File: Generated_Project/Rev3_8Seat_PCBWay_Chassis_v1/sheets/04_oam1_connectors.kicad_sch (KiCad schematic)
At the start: 0 parts

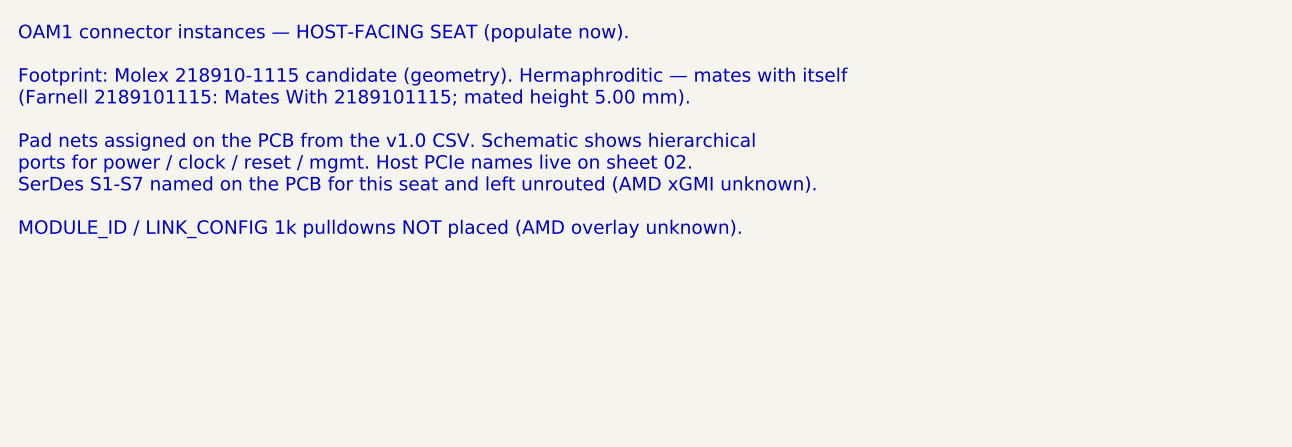
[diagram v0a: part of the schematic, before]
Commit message: Raise Rev3 chassis to 8 electrically designed seats.
Name v1.0 power/PE/clock nets on all eight OAM seats toward two DNP
PM8536B-FEI (x8 per GCD), keep SB175 star + local P48V pours, and generate
the 12-layer 2.0 mm stuffed-switch target. First stuffing may still populate
two modules; the PCB does not need a respin for the other six.

Do not fabricate. Do not energize P48V.

Co-authored-by: zivzancoeli-commits <zivzancoeli-commits@users.noreply.github.com>
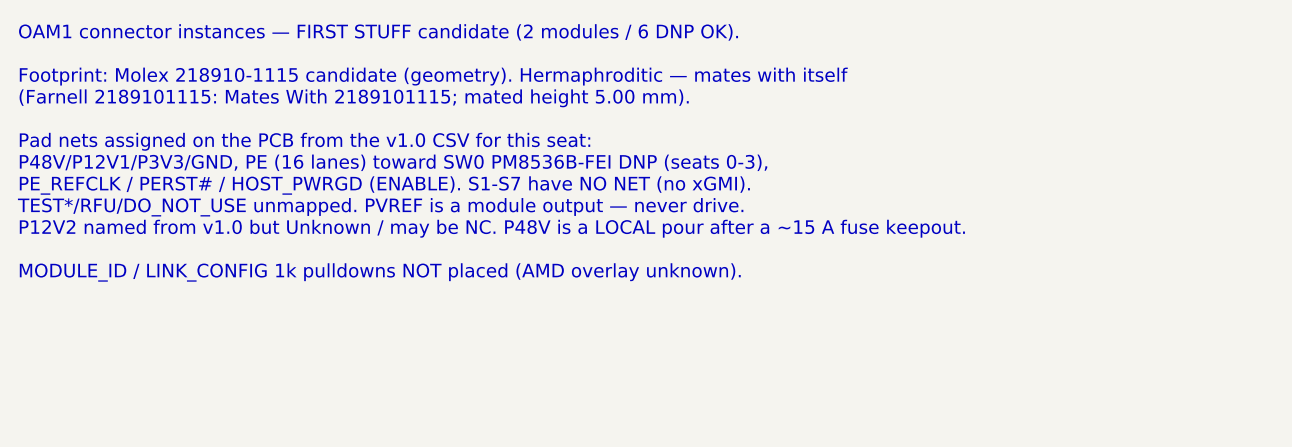
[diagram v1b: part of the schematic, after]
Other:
- note added: "OAM1 connector instances — FIRST STUFF candidate (2 modules / 6 DNP OK). Footprint: Molex 218910-1115 candidate (geometry). Hermaphroditic — mates with itself (Farnell 2189101115: Mates With 2189101115; mated height 5.00 mm). Pad nets assigned on the PCB from the v1.0 CSV for this seat: P48V/P12V1/P3V3/GND, PE (16 lanes) toward SW0 PM8536B-FEI DNP (seats 0-3), PE_REFCLK / PERST# / HOST_PWRGD (ENA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"
- note removed: "OAM1 connector instances — HOST-FACING SEAT (populate now). Footprint: Molex 218910-1115 candidate (geometry). Hermaphroditic — mates with itself (Farnell 2189101115: Mates With 2189101115; mated height 5.00 mm). Pad nets assigned on the PCB from the v1.0 CSV. Schematic shows hierarchical ports for power / clock / reset / mgmt. Host PCIe names live on sheet 02. SerDes S1-S7 named on the PCB for t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"
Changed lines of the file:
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@@
 		(date "2026-08-21")
 		(rev "Rev3_8Seat_PCBWay_v1")
-		(comment 1 "DO NOT FABRICATE. DO NOT ENERGIZE P48V. Ticket 167157 open.")
-		(comment 2 "Documentation sheet — no invented nets")
-		(comment 3 "Pin names: OAM Pin map rev 1.0.xlsx — OCP generic, NOT AMD overlay")
-		(comment 4 "r2.0 maps UNUSABLE. P3V3=2 Conn0 C1/C2. 8-seat PCBWay chassis stub.")
+        (comment 1 "DO NOT FABRICATE. DO NOT ENERGIZE P48V. Molex 60V written 2026-08-18; 1.2A/contact OPEN.")
+        (comment 2 "Documentation sheet — no invented nets")
+        (comment 3 "Pin names: OAM Pin map rev 1.0.xlsx — OCP generic, NOT AMD overlay")
+        (comment 4 "r2.0 UNUSABLE. P3V3=Conn0 C1/C2. 12L 2.0mm stuffed-switch TARGET. Star-fed P48V.")
 	)
-	(text "OAM1 connector instances — HOST-FACING SEAT (populate now).\n\nFootprint: Molex 218910-1115 candidate (geometry). Hermaphroditic — mates with itself\n(Farnell 2189101115: Mates With 2189101115; mated height 5.00 mm).\n\nPad nets assigned on the PCB from the v1.0 CSV. Schematic shows hierarchical\nports for power / clock / reset / mgmt. Host PCIe names live on sheet 02.\nSerDes S1-S7 named on the PCB for this seat and left unrouted (AMD xGMI unknown).\n\nMODULE_ID / LINK_CONFIG 1k pulldowns NOT placed (AMD overlay unknown).\n"
+	(text "OAM1 connector instances — FIRST STUFF candidate (2 modules / 6 DNP OK).\n\nFootprint: Molex 218910-1115 candidate (geometry). Hermaphroditic — mates with itself\n(Farnell 2189101115: Mates With 2189101115; mated height 5.00 mm).\n\nPad nets assigned on the PCB from the v1.0 CSV for this seat:\nP48V/P12V1/P3V3/GND, PE (16 lanes) toward SW0 PM8536B-FEI DNP (seats 0-3),\nPE_REFCLK / PERST# / HOST_PWRGD (ENABLE). S1-S7 have NO NET (no xGMI).\nTEST*/RFU/DO_NOT_USE unmapped. PVREF is a module output — never drive.\nP12V2 named from v1.0 but Unknown / may be NC. P48V is a LOCAL pour after a ~15 A fuse keepout.\n\nMODULE_ID / LINK_CONFIG 1k pulldowns NOT placed (AMD overlay unknown).\n"
 		(exclude_from_sim no)
 		(at 20.32 20.32 0)

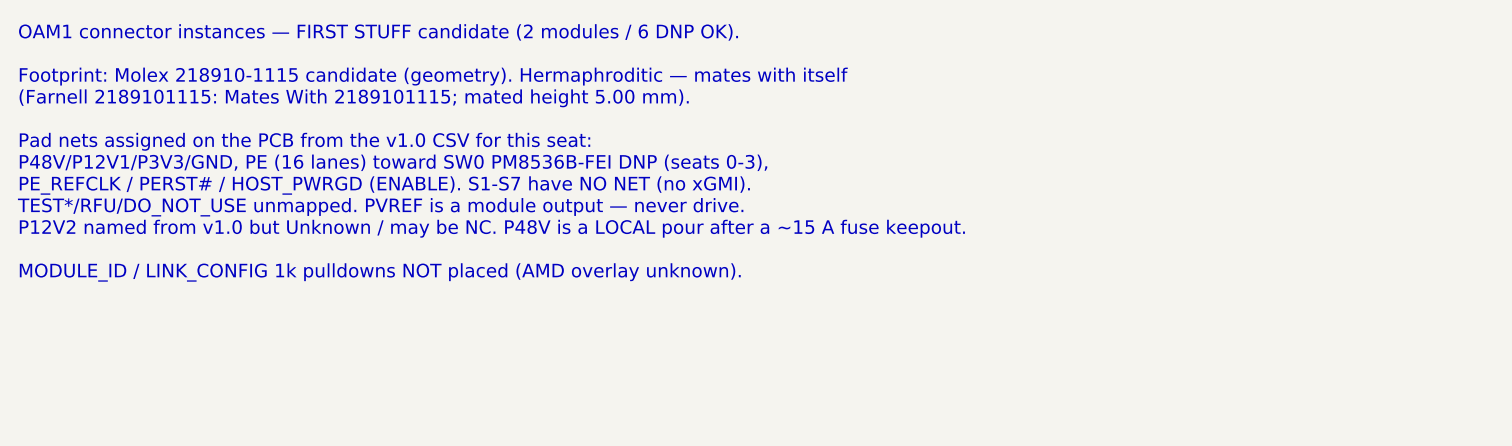
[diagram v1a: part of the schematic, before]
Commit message: Label PEX8780-AB80BI G as the only switch CANDIDATE (DNP).
Keepout is one 35 mm 1156-FCBGA for 8x x8 Gen3 plus one x16 host uplink.
Do not invent a second MPN. Do not stuff. 8-layer is likely if this BGA
is ever assembled; PCBWay 1156-FCBGA attach remains Unknown.

Still do not fabricate or energize P48V. No xGMI, no CEM.

Co-authored-by: zivzancoeli-commits <zivzancoeli-commits@users.noreply.github.com>
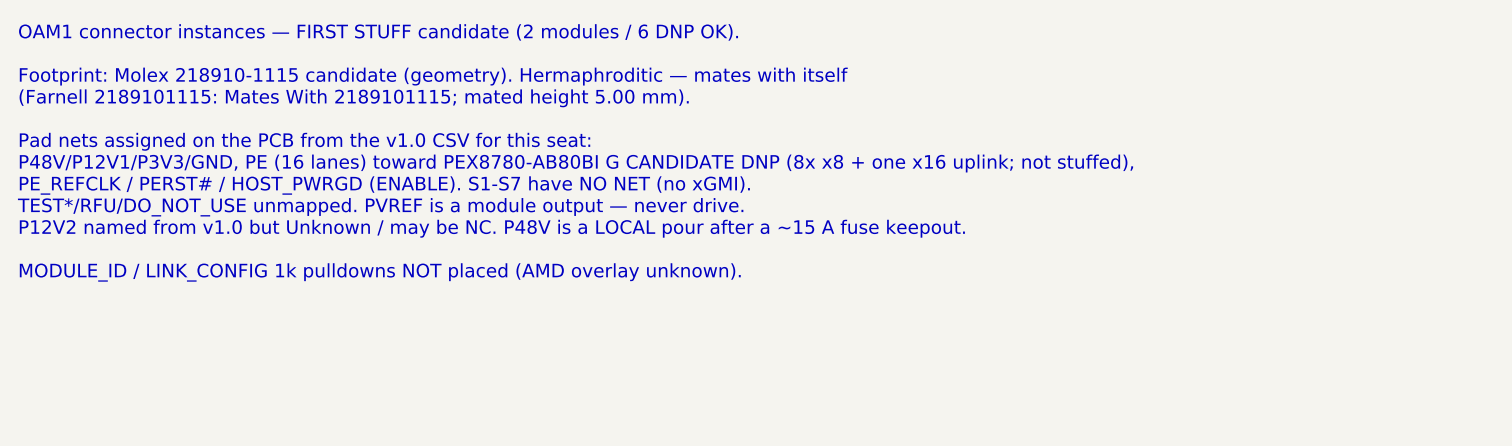
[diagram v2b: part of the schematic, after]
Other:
- note added: "OAM1 connector instances — FIRST STUFF candidate (2 modules / 6 DNP OK). Footprint: Molex 218910-1115 candidate (geometry). Hermaphroditic — mates with itself (Farnell 2189101115: Mates With 2189101115; mated height 5.00 mm). Pad nets assigned on the PCB from the v1.0 CSV for this seat: P48V/P12V1/P3V3/GND, PE (16 lanes) toward PEX8780-AB80BI G CANDIDATE DNP (8x x8 + one x16 uplink; not stuffed),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"
- note removed: "OAM1 connector instances — FIRST STUFF candidate (2 modules / 6 DNP OK). Footprint: Molex 218910-1115 candidate (geometry). Hermaphroditic — mates with itself (Farnell 2189101115: Mates With 2189101115; mated height 5.00 mm). Pad nets assigned on the PCB from the v1.0 CSV for this seat: P48V/P12V1/P3V3/GND, PE (16 lanes) toward SW0 PM8536B-FEI DNP (seats 0-3), PE_REFCLK / PERST# / HOST_PWRGD (ENA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"
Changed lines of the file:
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@@
         (comment 4 "r2.0 UNUSABLE. P3V3=Conn0 C1/C2. 12L 2.0mm stuffed-switch TARGET. Star-fed P48V.")
 	)
-	(text "OAM1 connector instances — FIRST STUFF candidate (2 modules / 6 DNP OK).\n\nFootprint: Molex 218910-1115 candidate (geometry). Hermaphroditic — mates with itself\n(Farnell 2189101115: Mates With 2189101115; mated height 5.00 mm).\n\nPad nets assigned on the PCB from the v1.0 CSV for this seat:\nP48V/P12V1/P3V3/GND, PE (16 lanes) toward SW0 PM8536B-FEI DNP (seats 0-3),\nPE_REFCLK / PERST# / HOST_PWRGD (ENABLE). S1-S7 have NO NET (no xGMI).\nTEST*/RFU/DO_NOT_USE unmapped. PVREF is a module output — never drive.\nP12V2 named from v1.0 but Unknown / may be NC. P48V is a LOCAL pour after a ~15 A fuse keepout.\n\nMODULE_ID / LINK_CONFIG 1k pulldowns NOT placed (AMD overlay unknown).\n"
+	(text "OAM1 connector instances — FIRST STUFF candidate (2 modules / 6 DNP OK).\n\nFootprint: Molex 218910-1115 candidate (geometry). Hermaphroditic — mates with itself\n(Farnell 2189101115: Mates With 2189101115; mated height 5.00 mm).\n\nPad nets assigned on the PCB from the v1.0 CSV for this seat:\nP48V/P12V1/P3V3/GND, PE (16 lanes) toward PEX8780-AB80BI G CANDIDATE DNP (8x x8 + one x16 uplink; not stuffed),\nPE_REFCLK / PERST# / HOST_PWRGD (ENABLE). S1-S7 have NO NET (no xGMI).\nTEST*/RFU/DO_NOT_USE unmapped. PVREF is a module output — never drive.\nP12V2 named from v1.0 but Unknown / may be NC. P48V is a LOCAL pour after a ~15 A fuse keepout.\n\nMODULE_ID / LINK_CONFIG 1k pulldowns NOT placed (AMD overlay unknown).\n"
 		(exclude_from_sim no)
 		(at 20.32 20.32 0)

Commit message: Make PM8536B-FEI the PRIMARY switch keepout (DNP x2).
Two 37.5 mm 1311-FCBGA courtyards, x8 per GCD (SW0 seats 0-3, SW1 4-7),
two CPU x16 uplinks. PEX8780 stays a cheaper 80-lane alt in docs only.
GCD1 = SERDES_7 remains Inferred. No CEM, no xGMI, do not fabricate.

Co-authored-by: zivzancoeli-commits <zivzancoeli-commits@users.noreply.github.com>
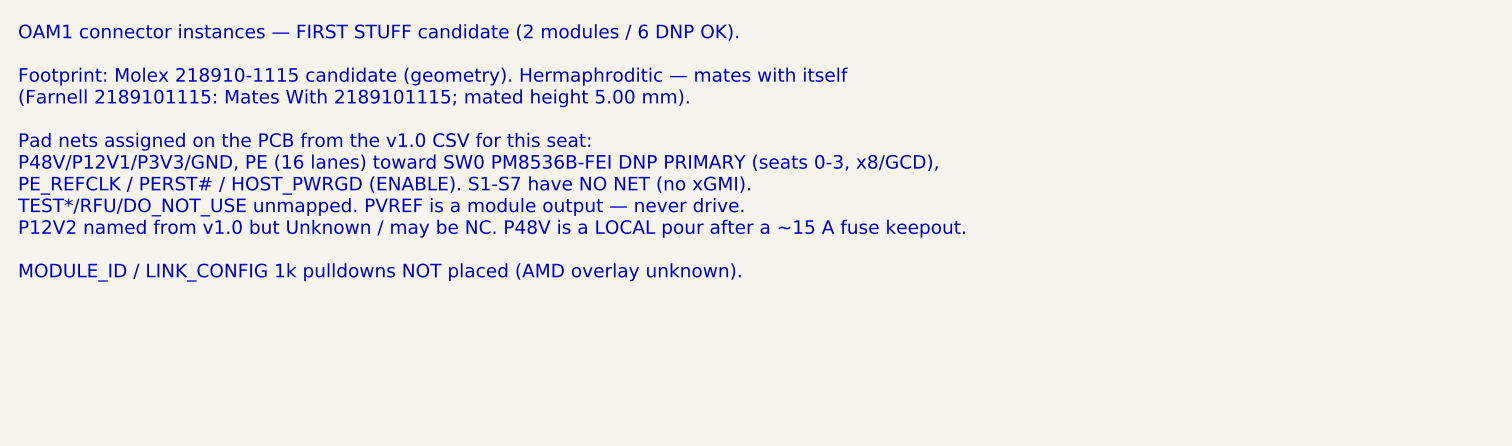
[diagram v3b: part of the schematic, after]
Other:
- note added: "OAM1 connector instances — FIRST STUFF candidate (2 modules / 6 DNP OK). Footprint: Molex 218910-1115 candidate (geometry). Hermaphroditic — mates with itself (Farnell 2189101115: Mates With 2189101115; mated height 5.00 mm). Pad nets assigned on the PCB from the v1.0 CSV for this seat: P48V/P12V1/P3V3/GND, PE (16 lanes) toward SW0 PM8536B-FEI DNP PRIMARY (seats 0-3, x8/GCD), PE_REFCLK / PERST# /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"
- note removed: "OAM1 connector instances — FIRST STUFF candidate (2 modules / 6 DNP OK). Footprint: Molex 218910-1115 candidate (geometry). Hermaphroditic — mates with itself (Farnell 2189101115: Mates With 2189101115; mated height 5.00 mm). Pad nets assigned on the PCB from the v1.0 CSV for this seat: P48V/P12V1/P3V3/GND, PE (16 lanes) toward PEX8780-AB80BI G CANDIDATE DNP (8x x8 + one x16 uplink; not stuffed),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"
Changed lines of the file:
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@@
         (comment 2 "Documentation sheet — no invented nets")
         (comment 3 "Pin names: OAM Pin map rev 1.0.xlsx — OCP generic, NOT AMD overlay")
-        (comment 4 "r2.0 UNUSABLE. P3V3=Conn0 C1/C2. 12L 2.0mm stuffed-switch TARGET. Star-fed P48V.")
+        (comment 4 "r2.0 UNUSABLE. P3V3=Conn0 C1/C2. 12L 2.0mm stuffed-switch TARGET. 2x PM8536 DNP. Star-fed P48V.")
 	)
-	(text "OAM1 connector instances — FIRST STUFF candidate (2 modules / 6 DNP OK).\n\nFootprint: Molex 218910-1115 candidate (geometry). Hermaphroditic — mates with itself\n(Farnell 2189101115: Mates With 2189101115; mated height 5.00 mm).\n\nPad nets assigned on the PCB from the v1.0 CSV for this seat:\nP48V/P12V1/P3V3/GND, PE (16 lanes) toward PEX8780-AB80BI G CANDIDATE DNP (8x x8 + one x16 uplink; not stuffed),\nPE_REFCLK / PERST# / HOST_PWRGD (ENABLE). S1-S7 have NO NET (no xGMI).\nTEST*/RFU/DO_NOT_USE unmapped. PVREF is a module output — never drive.\nP12V2 named from v1.0 but Unknown / may be NC. P48V is a LOCAL pour after a ~15 A fuse keepout.\n\nMODULE_ID / LINK_CONFIG 1k pulldowns NOT placed (AMD overlay unknown).\n"
+	(text "OAM1 connector instances — FIRST STUFF candidate (2 modules / 6 DNP OK).\n\nFootprint: Molex 218910-1115 candidate (geometry). Hermaphroditic — mates with itself\n(Farnell 2189101115: Mates With 2189101115; mated height 5.00 mm).\n\nPad nets assigned on the PCB from the v1.0 CSV for this seat:\nP48V/P12V1/P3V3/GND, PE (16 lanes) toward SW0 PM8536B-FEI DNP PRIMARY (seats 0-3, x8/GCD),\nPE_REFCLK / PERST# / HOST_PWRGD (ENABLE). S1-S7 have NO NET (no xGMI).\nTEST*/RFU/DO_NOT_USE unmapped. PVREF is a module output — never drive.\nP12V2 named from v1.0 but Unknown / may be NC. P48V is a LOCAL pour after a ~15 A fuse keepout.\n\nMODULE_ID / LINK_CONFIG 1k pulldowns NOT placed (AMD overlay unknown).\n"
 		(exclude_from_sim no)
 		(at 20.32 20.32 0)

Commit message: Make the Rev3 8-seat chassis full-width capable with four PM8536 DNP courtyards.
Same 492x372 POWER+MECH PCB; architecture is now 16 named x16 PE buses
(PE_Sn_GCD0_x16 + PE_Sn_GCD1_x16) and SW0-SW3 keepouts. Two 96-lane
switches are enough for 8x x8/GCD, not 8x x16/GCD. Host stays X11DPH-T
(~80 lanes) and cannot light 256 downstream. Do not energize P48V.

Co-authored-by: zivzancoeli-commits <zivzancoeli-commits@users.noreply.github.com>
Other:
- note added: "OAM1 connector instances — FIRST STUFF (populate path 2: seats 0-1; stuff SW0 later). Footprint: Molex 218910-1115 candidate (geometry). Hermaphroditic — mates with itself (Farnell 2189101115: Mates With 2189101115; mated height 5.00 mm). Pad nets assigned on the PCB from the v1.0 CSV for this seat: P48V/P12V1/P3V3/GND, Conn0 PE 16 lanes (PE_S1_GCD0_x16) toward SW0 PM8536B-FEI DNP (seats 0,1, 16 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"
- note removed: "OAM1 connector instances — FIRST STUFF candidate (2 modules / 6 DNP OK). Footprint: Molex 218910-1115 candidate (geometry). Hermaphroditic — mates with itself (Farnell 2189101115: Mates With 2189101115; mated height 5.00 mm). Pad nets assigned on the PCB from the v1.0 CSV for this seat: P48V/P12V1/P3V3/GND, PE (16 lanes) toward SW0 PM8536B-FEI DNP PRIMARY (seats 0-3, x8/GCD), PE_REFCLK / PERST# /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"
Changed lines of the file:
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@@
         (comment 2 "Documentation sheet — no invented nets")
         (comment 3 "Pin names: OAM Pin map rev 1.0.xlsx — OCP generic, NOT AMD overlay")
-        (comment 4 "r2.0 UNUSABLE. P3V3=Conn0 C1/C2. 12L 2.0mm stuffed-switch TARGET. 2x PM8536 DNP. Star-fed P48V.")
+        (comment 4 "r2.0 UNUSABLE. P3V3=Conn0 C1/C2. 12L 2.0mm stuffed-switch TARGET. 4x PM8536 DNP. Star-fed P48V.")
 	)
-	(text "OAM1 connector instances — FIRST STUFF candidate (2 modules / 6 DNP OK).\n\nFootprint: Molex 218910-1115 candidate (geometry). Hermaphroditic — mates with itself\n(Farnell 2189101115: Mates With 2189101115; mated height 5.00 mm).\n\nPad nets assigned on the PCB from the v1.0 CSV for this seat:\nP48V/P12V1/P3V3/GND, PE (16 lanes) toward SW0 PM8536B-FEI DNP PRIMARY (seats 0-3, x8/GCD),\nPE_REFCLK / PERST# / HOST_PWRGD (ENABLE). S1-S7 have NO NET (no xGMI).\nTEST*/RFU/DO_NOT_USE unmapped. PVREF is a module output — never drive.\nP12V2 named from v1.0 but Unknown / may be NC. P48V is a LOCAL pour after a ~15 A fuse keepout.\n\nMODULE_ID / LINK_CONFIG 1k pulldowns NOT placed (AMD overlay unknown).\n"
+	(text "OAM1 connector instances — FIRST STUFF (populate path 2: seats 0-1; stuff SW0 later).\n\nFootprint: Molex 218910-1115 candidate (geometry). Hermaphroditic — mates with itself\n(Farnell 2189101115: Mates With 2189101115; mated height 5.00 mm).\n\nPad nets assigned on the PCB from the v1.0 CSV for this seat:\nP48V/P12V1/P3V3/GND, Conn0 PE 16 lanes (PE_S1_GCD0_x16) toward SW0 PM8536B-FEI DNP\n(seats 0,1, 16 US + 64 DS hypothesis — not a ball map),\nPE_S1_GCD1_x16 named-only (pins Unknown; not S1-S7),\nPE_REFCLK / PERST# / HOST_PWRGD (ENABLE). S1-S7 have NO NET (no xGMI).\nTEST*/RFU/DO_NOT_USE unmapped. PVREF is a module output — never drive.\nP12V2 named from v1.0 but Unknown / may be NC. P48V is a LOCAL pour after a ~15 A fuse keepout.\n\nMODULE_ID / LINK_CONFIG 1k pulldowns NOT placed (AMD overlay unknown).\n"
 		(exclude_from_sim no)
 		(at 20.32 20.32 0)
@@
 		(effects (font (size 1.27 1.27)) (justify left))
 	)
+	(hierarchical_label "PE_S1_GCD0_x16"
+		(shape bidirectional)
+		(at 25.4 231.2800000000002 0)
+		(effects (font (size 1.27 1.27)) (justify left))
+	)
+	(hierarchical_label "PE_S1_GCD1_x16"
+		(shape bidirectional)
+		(at 25.4 236.3600000000002 0)
+		(effects (font (size 1.27 1.27)) (justify left))
+	)
